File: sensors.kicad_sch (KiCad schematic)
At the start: 10 parts, among them J2 S4B-XH-A, Q2 BSS138, U1 ICM-42688-P

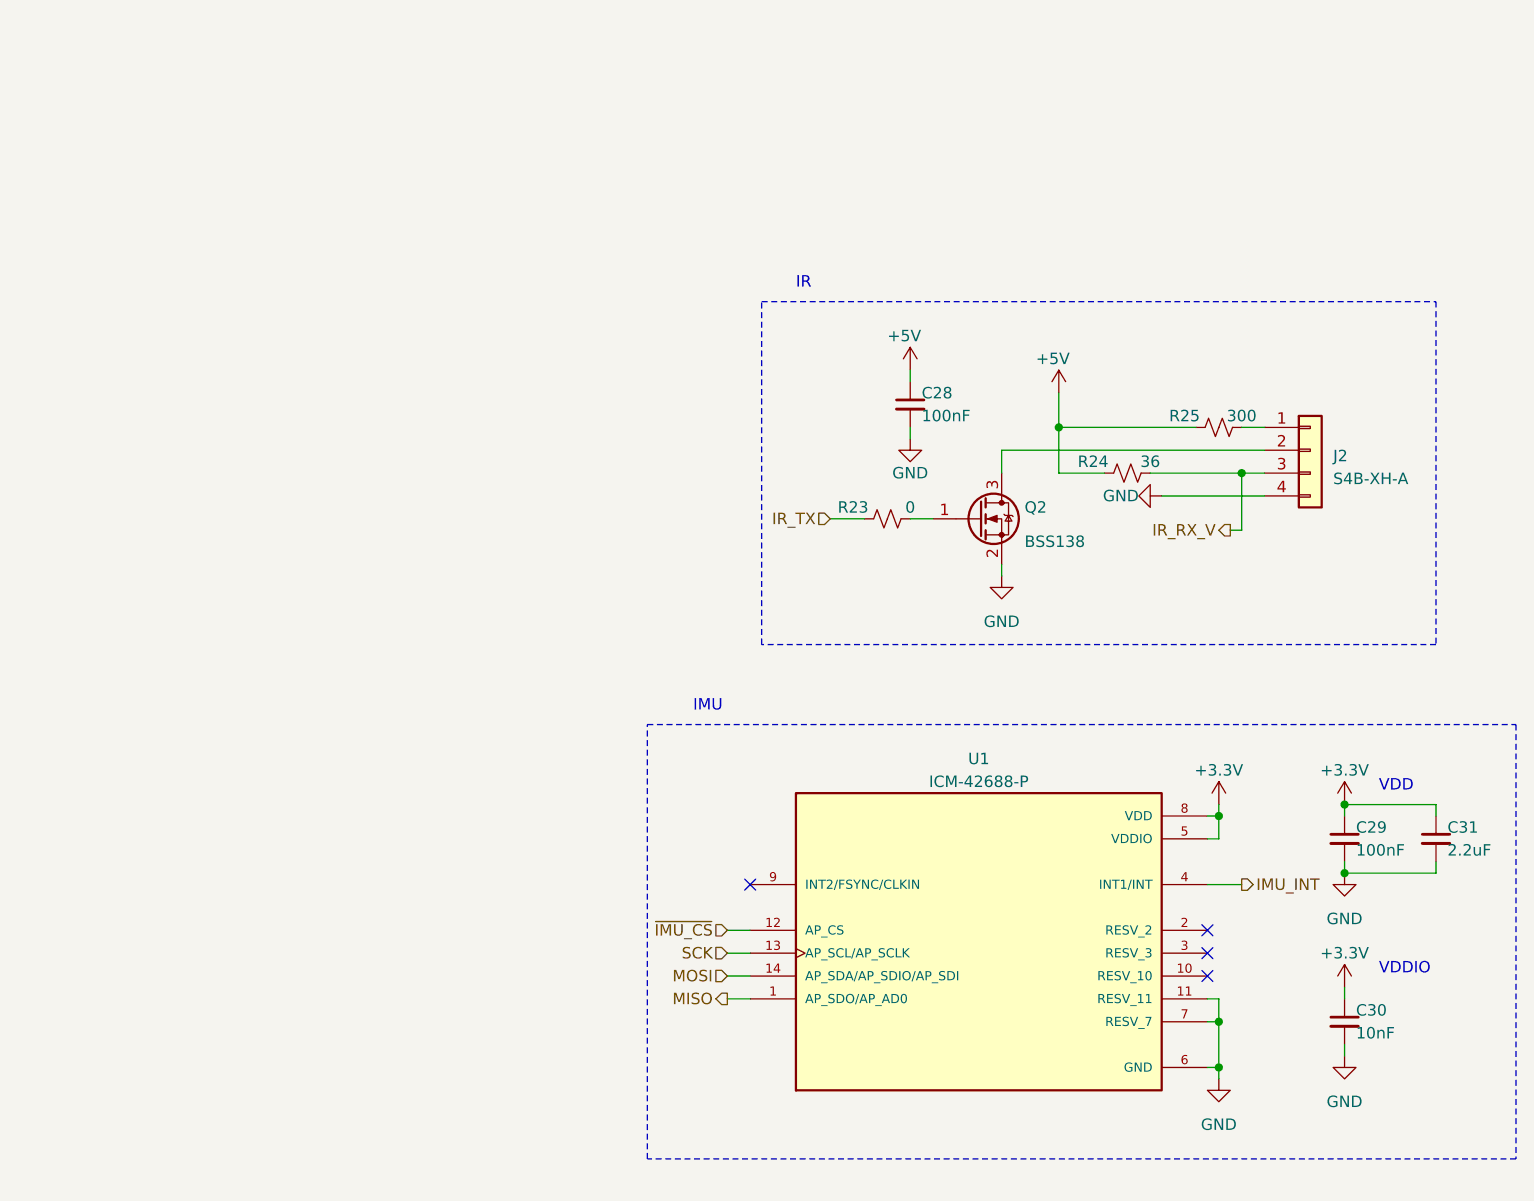
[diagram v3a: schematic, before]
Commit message: Finish connecting everything in sch.
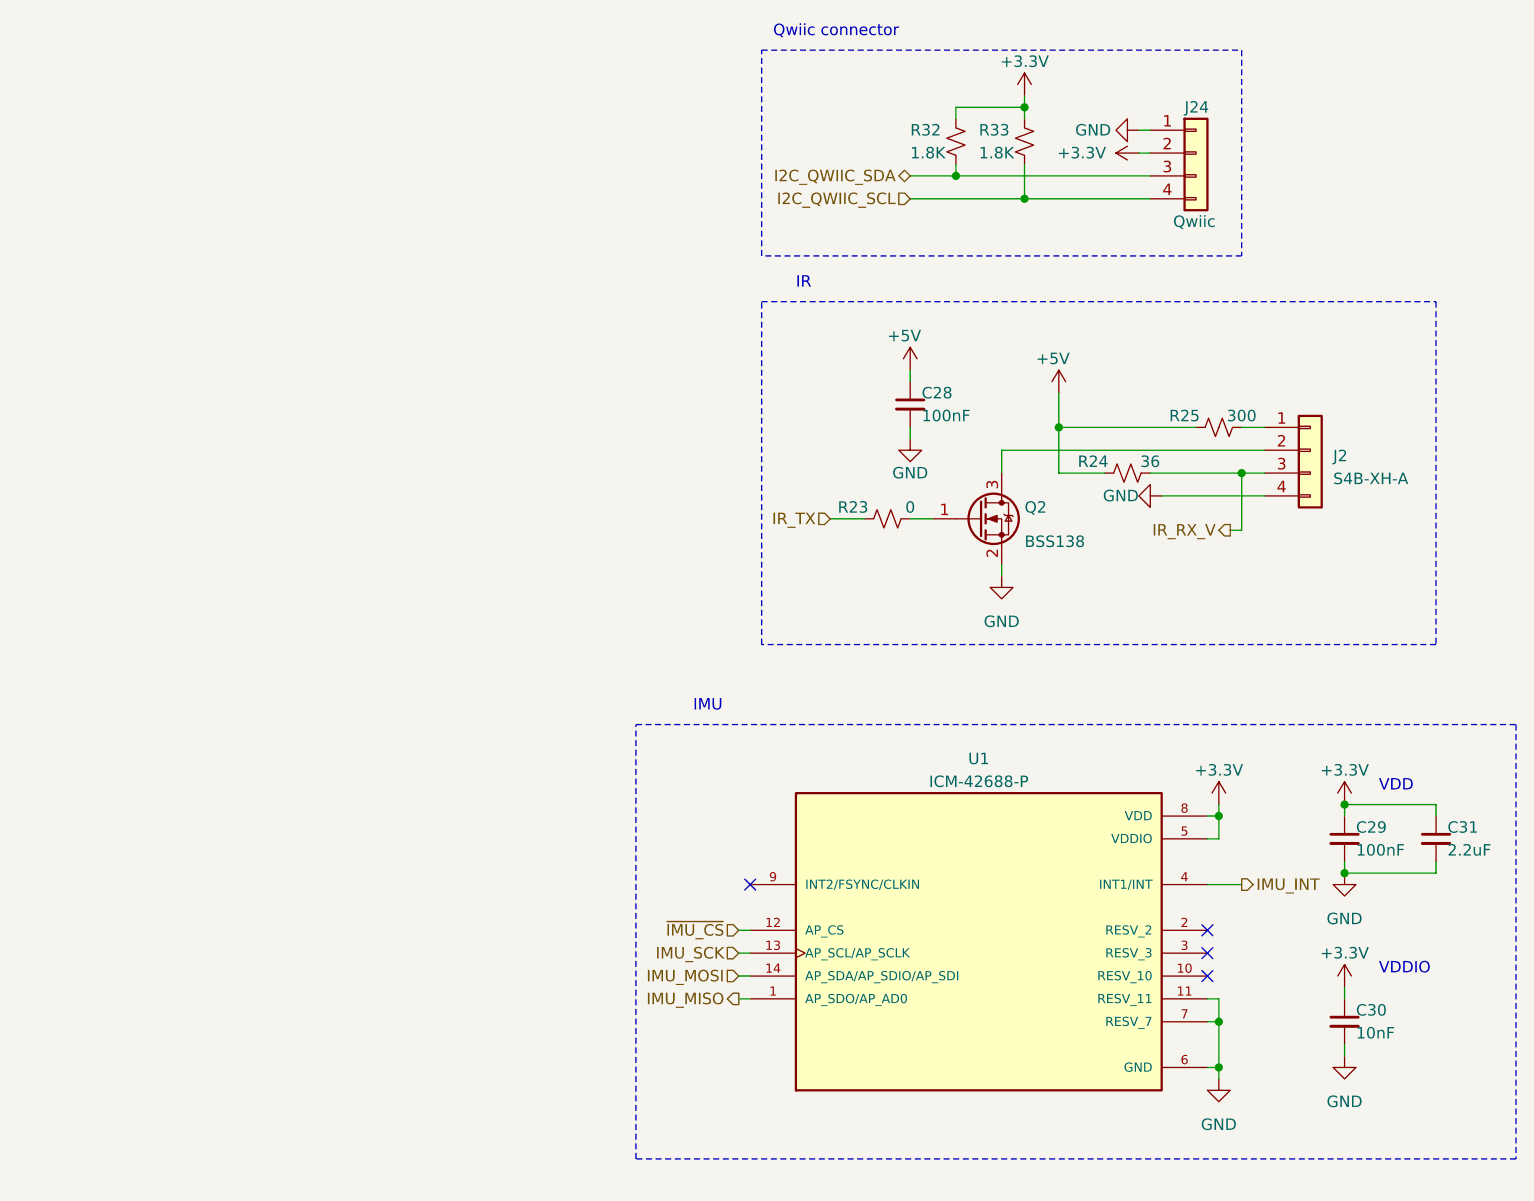
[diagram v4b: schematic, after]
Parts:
- added J24: Qwiic, Connector_JST:JST_SH_SM04B-SRSS-TB_1x04-1MP_P1.00mm_Horizontal, symbol Connector_Generic:Conn_01x04
- added R32, R33: 1.8K, symbol Device:R_Small_US
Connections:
- net +3.3V: now also J24.2 (Pin_2), R32.1, R33.1
- net GND: now also J24.1 (Pin_1)
- net MISO renamed IMU_MISO
- net MOSI renamed IMU_MOSI
- net SCK renamed IMU_SCK
- new net I2C_QWIIC_SCL: J24.4 (Pin_4), R33.2
- new net I2C_QWIIC_SDA: J24.3 (Pin_3), R32.2
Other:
- note added: "Qwiic connector"

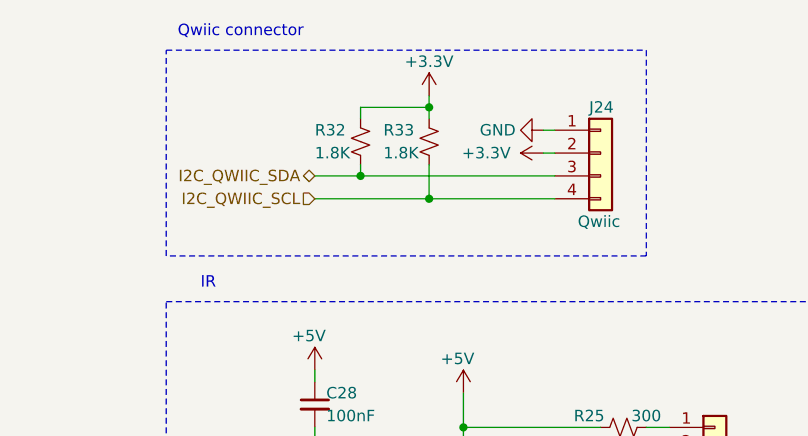
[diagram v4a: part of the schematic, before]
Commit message: Assign some of the footprints and MPNs.
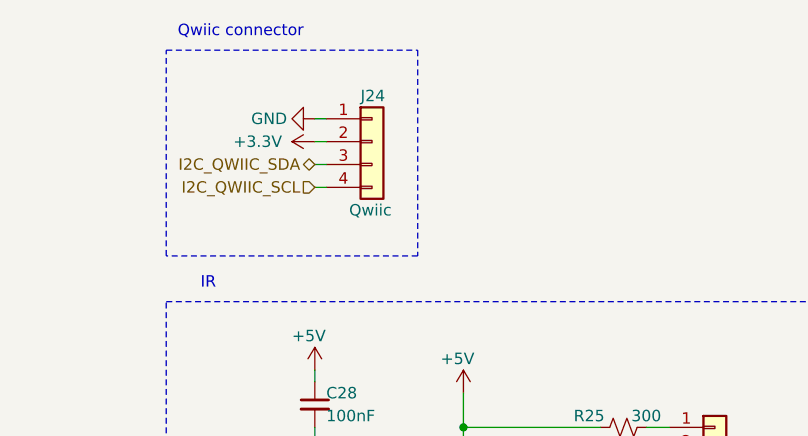
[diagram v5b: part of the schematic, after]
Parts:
- removed R32, R33: 1.8K, symbol Device:R_Small_US
- C28, C29, C30: footprint (none) -> Capacitor_SMD:C_0402_1005Metric
- J2: footprint (none) -> Connector_JST:JST_XH_S4B-XH-A_1x04_P2.50mm_Horizontal; MPN (none) -> S4B-XH-A(LF)(SN)
- R23, R24, R25: footprint (none) -> Resistor_SMD:R_0402_1005Metric
- U1: MANUFACTURER TDK InvenSense -> (none); MAXIMUM_PACKAGE_HEIGHT 0.97mm -> (none); PARTREV 1.2 -> (none); STANDARD IPC-7351B -> (none)
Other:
- moved on the sheet: J24

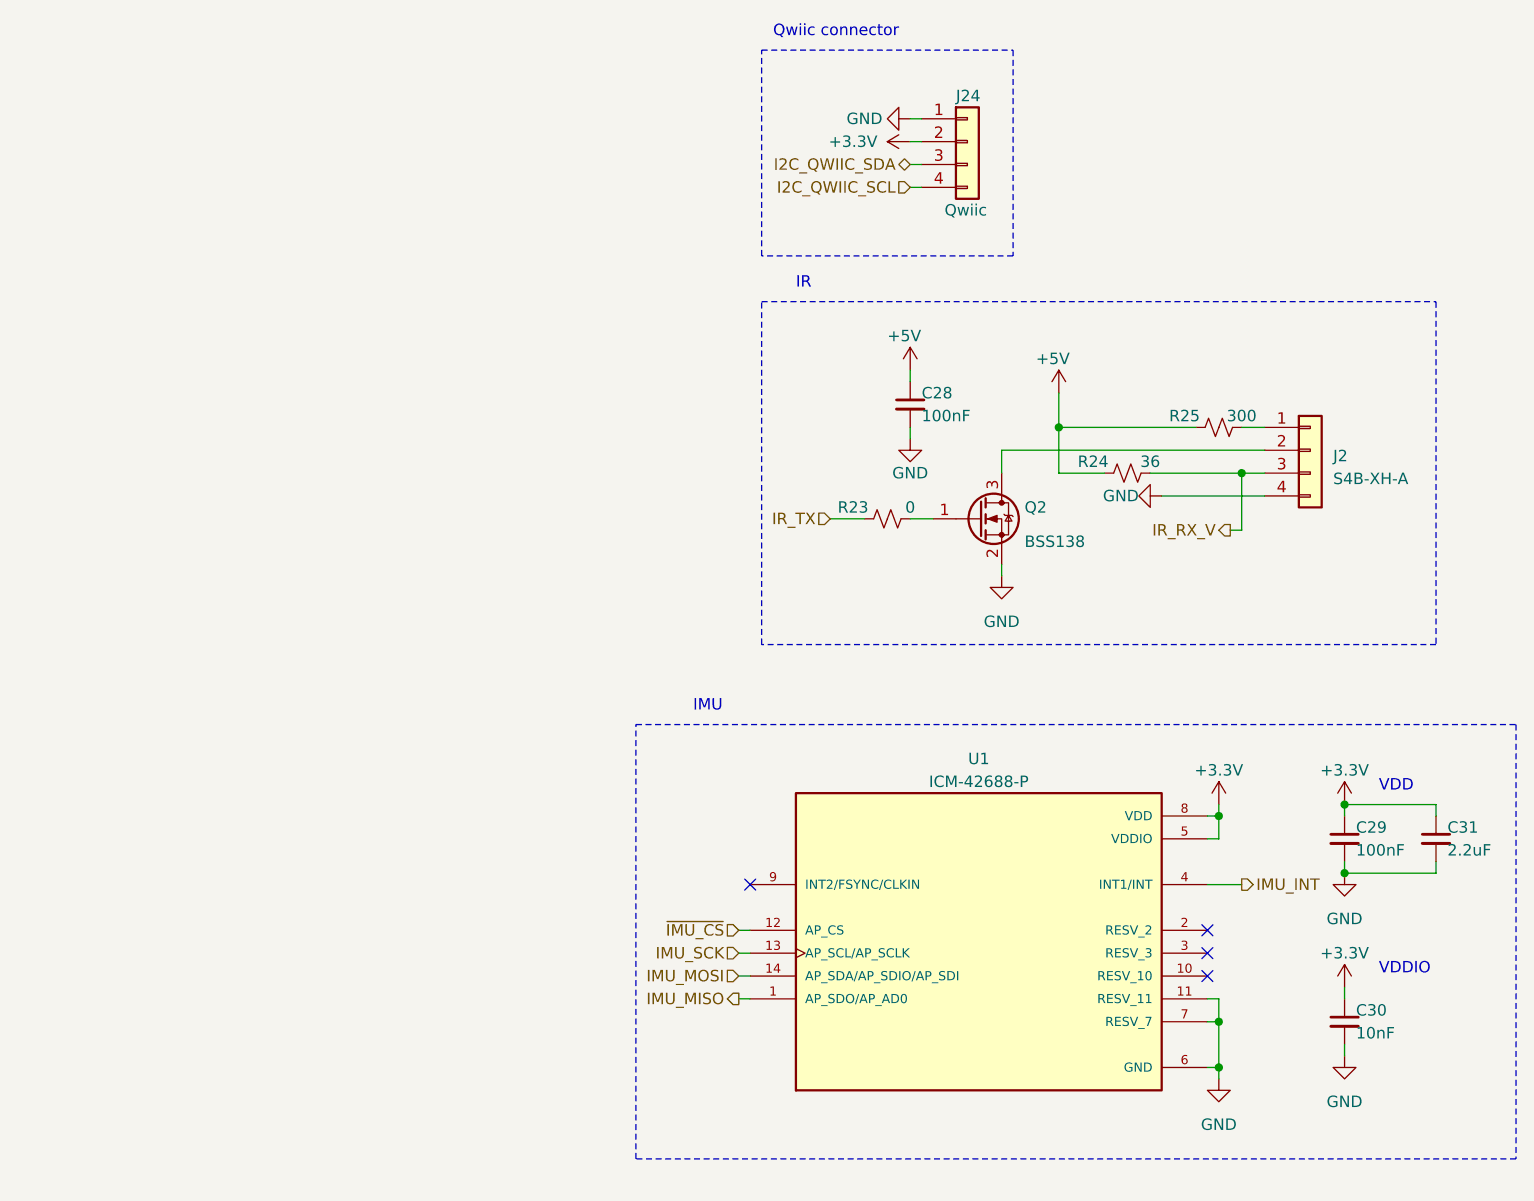
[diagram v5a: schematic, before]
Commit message: Import the previous main board to match the overall shape, and re-annotate the schematic.
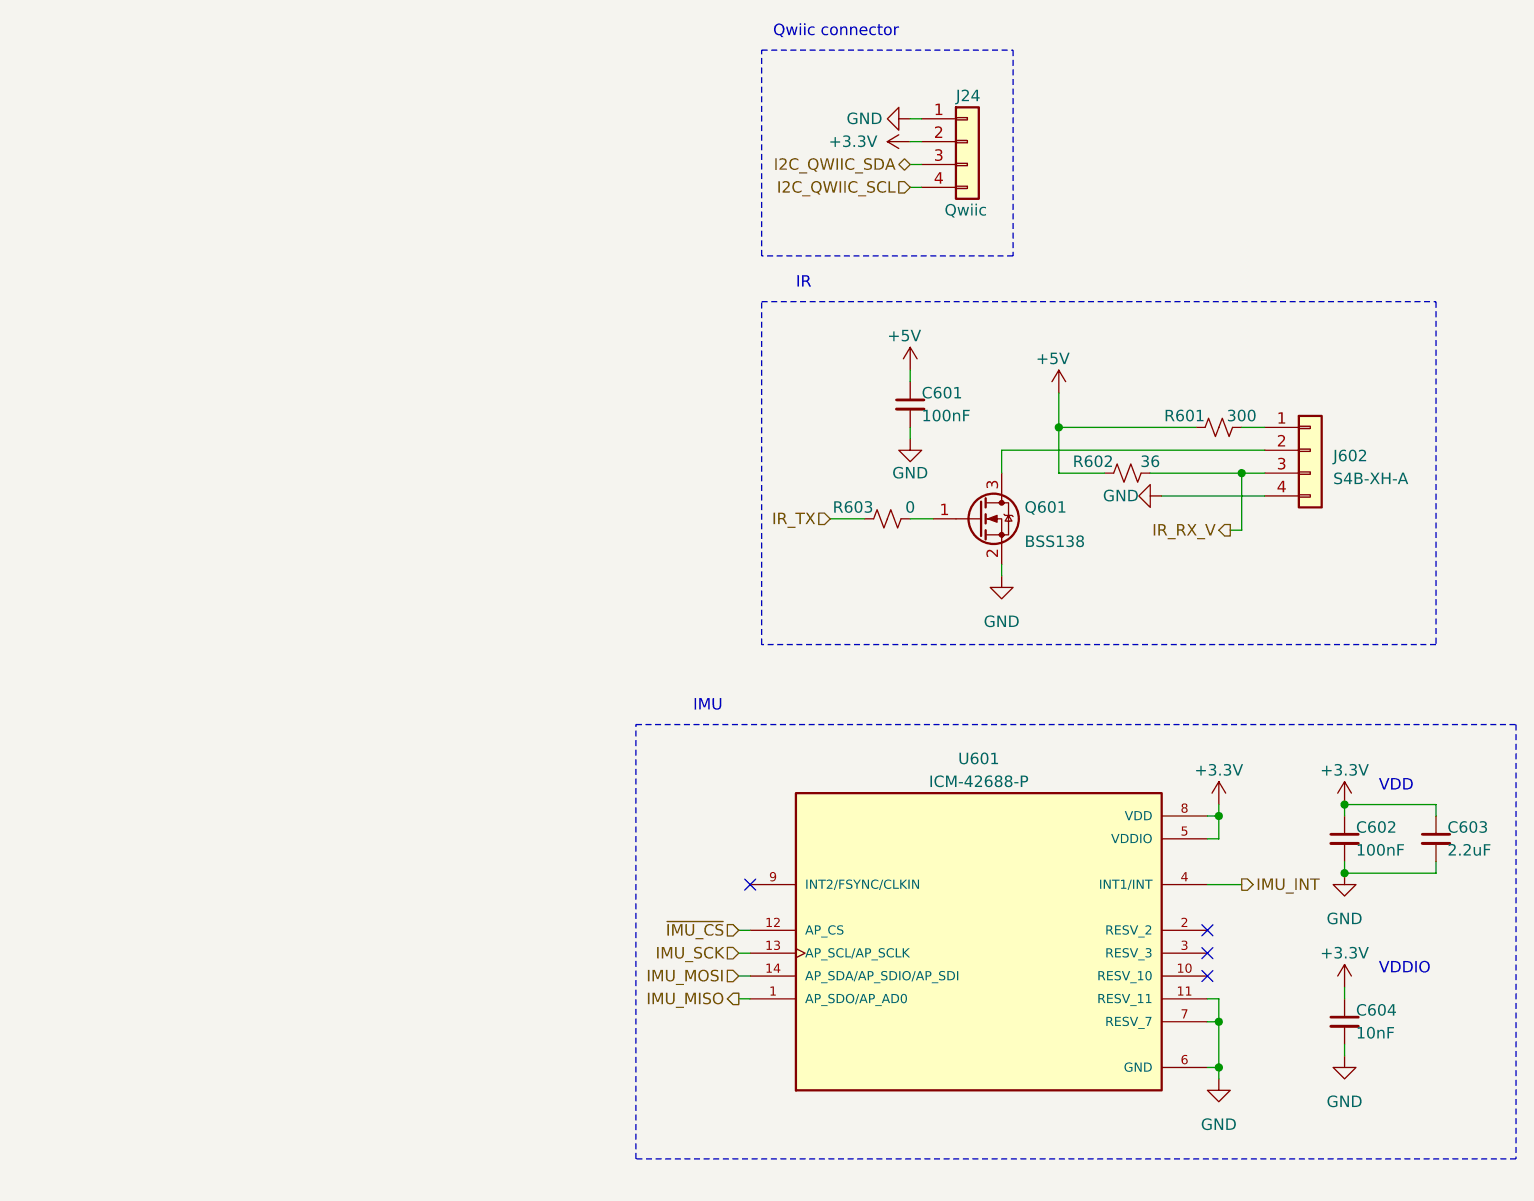
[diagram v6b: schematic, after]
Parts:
- C601: renamed from C28; footprint Capacitor_SMD:C_0402_1005Metric -> Capacitor_SMD:C_0603_1608Metric; MPN (none) -> RM EMK105 B7104KV-F
- C602: renamed from C29; footprint Capacitor_SMD:C_0402_1005Metric -> Capacitor_SMD:C_0603_1608Metric; MPN (none) -> RM EMK105 B7104KV-F
- C603: renamed from C31; footprint (none) -> Capacitor_SMD:C_0805_2012Metric
- C604: renamed from C30; footprint Capacitor_SMD:C_0402_1005Metric -> Capacitor_SMD:C_0603_1608Metric
- R601: renamed from R25; footprint Resistor_SMD:R_0402_1005Metric -> Resistor_SMD:R_0603_1608Metric
- R602: renamed from R24; footprint Resistor_SMD:R_0402_1005Metric -> Resistor_SMD:R_0603_1608Metric
- R603: renamed from R23; footprint Resistor_SMD:R_0402_1005Metric -> Resistor_SMD:R_0603_1608Metric; MPN (none) -> RMCF0603ZT0R00
- renumbered J2 to J602, Q2 to Q601, U1 to U601

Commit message: Place all the components on the PCB.
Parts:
- J24: MPN (none) -> SM04B-SRSS-TB(LF)(SN)
- J602: value S4B-XH-A -> IR; footprint Connector_JST:JST_XH_S4B-XH-A_1x04_P2.50mm_Horizontal -> Connector_JST:JST_SH_SM04B-SRSS-TB_1x04-1MP_P1.00mm_Horizontal; MPN S4B-XH-A(LF)(SN) -> SM04B-SRSS-TB(LF)(SN)
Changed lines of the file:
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@@
   )
   (symbol (lib_id "Connector_Generic:Conn_01x04") (at 237.49 73.66 0) (unit 1)
-    (in_bom yes) (on_board yes) (dnp no) (fields_autoplaced)
-    (property "Reference" "J602" (at 240.03 74.295 0)
-      (effects (font (size 1.27 1.27)) (justify left))
-    )
-    (property "Value" "S4B-XH-A" (at 240.03 76.835 0)
-      (effects (font (size 1.27 1.27)) (justify left))
-    )
-    (property "Footprint" "Connector_JST:JST_XH_S4B-XH-A_1x04_P2.50mm_Horizontal" (at 237.49 73.66 0)
+    (in_bom yes) (on_board yes) (dnp no)
+    (property "Reference" "J602" (at 234.95 68.58 0)
+      (effects (font (size 1.27 1.27)) (justify left))
+    )
+    (property "Value" "IR" (at 236.22 81.28 0)
+      (effects (font (size 1.27 1.27)) (justify left))
+    )
+    (property "Footprint" "Connector_JST:JST_SH_SM04B-SRSS-TB_1x04-1MP_P1.00mm_Horizontal" (at 237.49 73.66 0)
       (effects (font (size 1.27 1.27)) hide)
     )
@@
       (effects (font (size 1.27 1.27)) hide)
     )
-    (property "MPN" "S4B-XH-A(LF)(SN)" (at 237.49 73.66 0)
+    (property "MPN" "SM04B-SRSS-TB(LF)(SN)" (at 237.49 73.66 0)
       (effects (font (size 1.27 1.27)) hide)
     )
@@
   (symbol (lib_id "Connector_Generic:Conn_01x04") (at 199.39 39.37 0) (unit 1)
     (in_bom yes) (on_board yes) (dnp no)
-    (property "Reference" "J24" (at 198.12 34.29 0)
+    (property "Reference" "J24" (at 196.85 34.29 0)
       (effects (font (size 1.27 1.27)) (justify left))
     )
@@
       (effects (font (size 1.27 1.27)) hide)
     )
+    (property "MPN" "SM04B-SRSS-TB(LF)(SN)" (at 199.39 39.37 0)
+      (effects (font (size 1.27 1.27)) hide)
+    )
